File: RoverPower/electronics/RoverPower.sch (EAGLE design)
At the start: 19 parts, among them IC1 INA168, IC3 TINY85, J1 I2C/ISP, U2 L7805

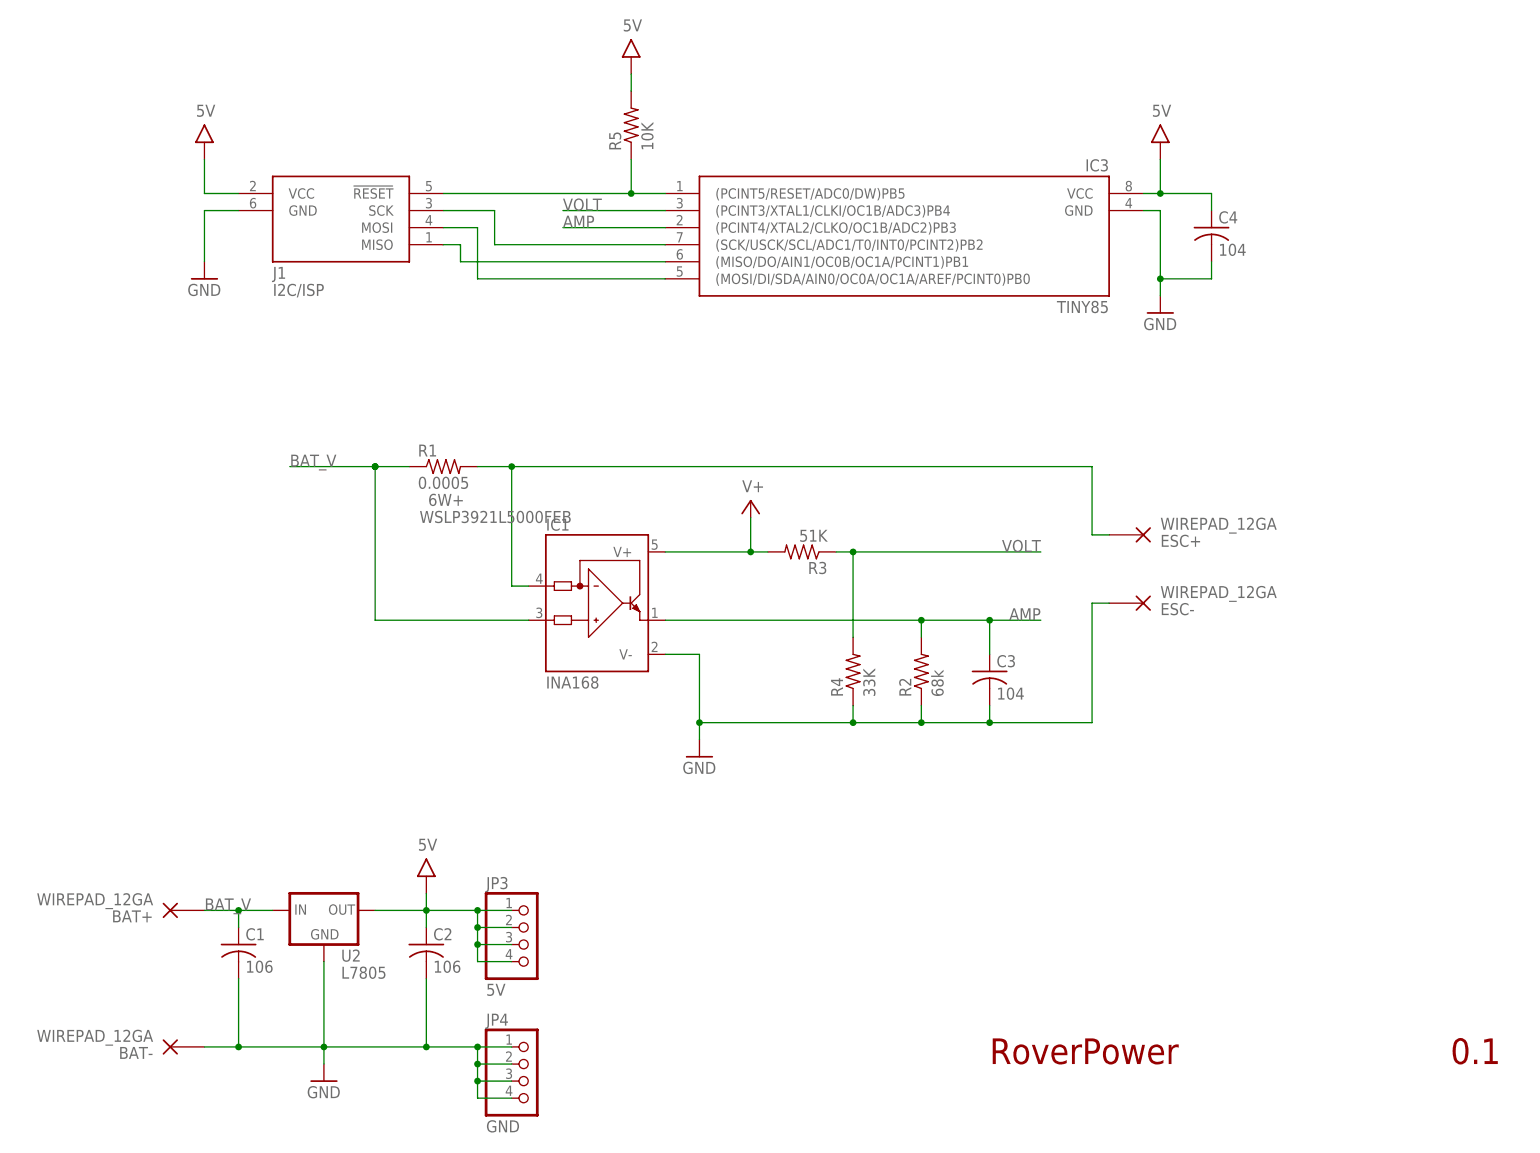
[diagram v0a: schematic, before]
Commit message: Revised traces between bat/esc, added stop mask for tinning. Shrank board size significantly. Added labeling.
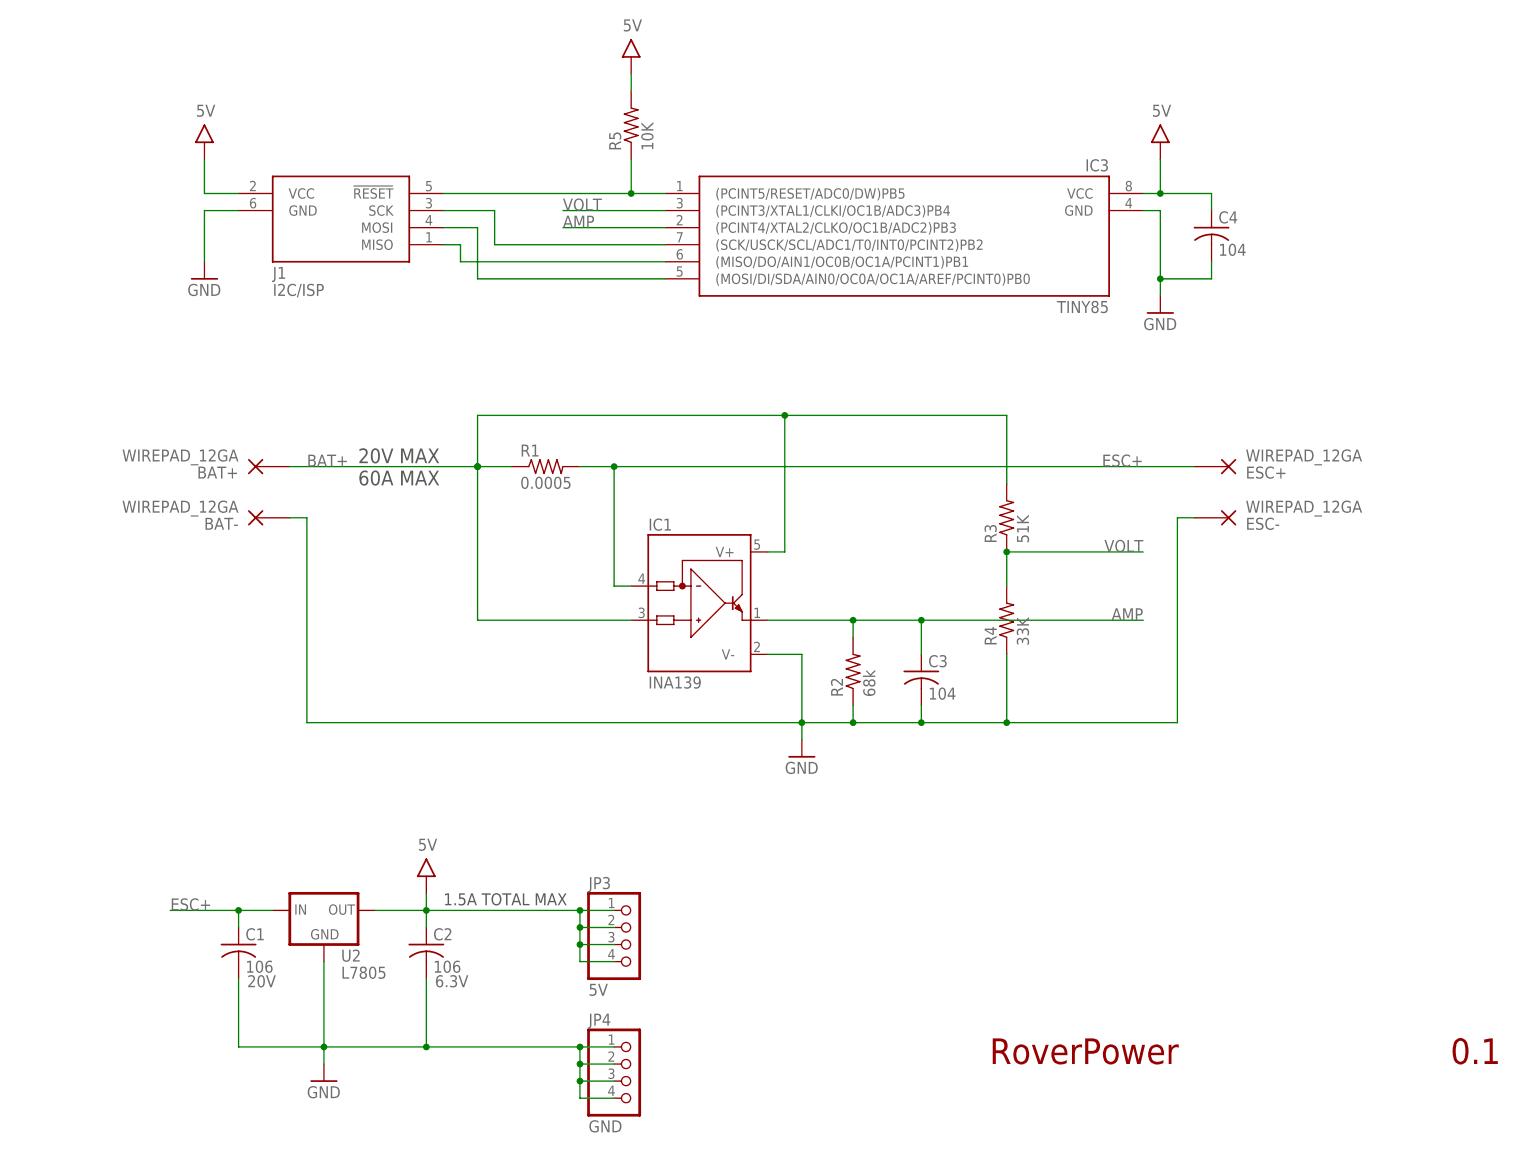
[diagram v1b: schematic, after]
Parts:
- C1: VOLTAGE (none) -> 20V
- C2: VOLTAGE (none) -> 6.3V
- IC1: value INA168 -> INA139
- R1: device bt:R-US__3921 -> bt:R-US__2512; PARTNO WSLP3921L5000FEB -> (none); POWER 6W+ -> (none)
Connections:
- removed net BAT_V: BAT+.P, C1.1, IC1.IN+, R1.1, U2.IN
- removed net ESC_V: ESC+.P, IC1.IN-, R1.2
- removed net V+: IC1.V+, R3.2
- new net BAT+: BAT+.P, IC1.IN+, IC1.V+, R1.1, R3.2
- new net ESC+: C1.1, ESC+.P, IC1.IN-, R1.2, U2.IN
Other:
- note added: "1.5A TOTAL MAX"
- note added: "20V MAX"
- note added: "60A MAX"
- moved on the sheet: BAT+, BAT-, C3, ESC+, ESC-, IC1, JP3, JP4, R1, R2, R3, R4

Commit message: Fixed Tiny label
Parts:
- IC3: value TINY85 -> TINY25
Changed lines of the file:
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@@
 <part name="U$2" library="bt" deviceset="5V" device=""/>
 <part name="GND3" library="bt" deviceset="GND" device=""/>
-<part name="IC3" library="bt_avr" deviceset="TINY25/45/85" device="-20SU" value="TINY85"/>
+<part name="IC3" library="bt_avr" deviceset="TINY25/45/85" device="-20SU" value="TINY25"/>
 <part name="U$3" library="bt" deviceset="5V" device=""/>
 <part name="GND4" library="bt" deviceset="GND" device=""/>
